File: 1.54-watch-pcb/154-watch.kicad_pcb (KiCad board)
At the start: 4 copper layers, 50 x 32.5 mm, 58 parts, among them J1 AFC24-S24FIC-00, J2 Conn_01x06_Female, J3 USB_C_Programming, J4 Jack-DC, J5 Conn_01x02_Male, Q1 Si1308, Q2 BC817, Q3 BC817, Q4 Si2301CDS, SW1 RESET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

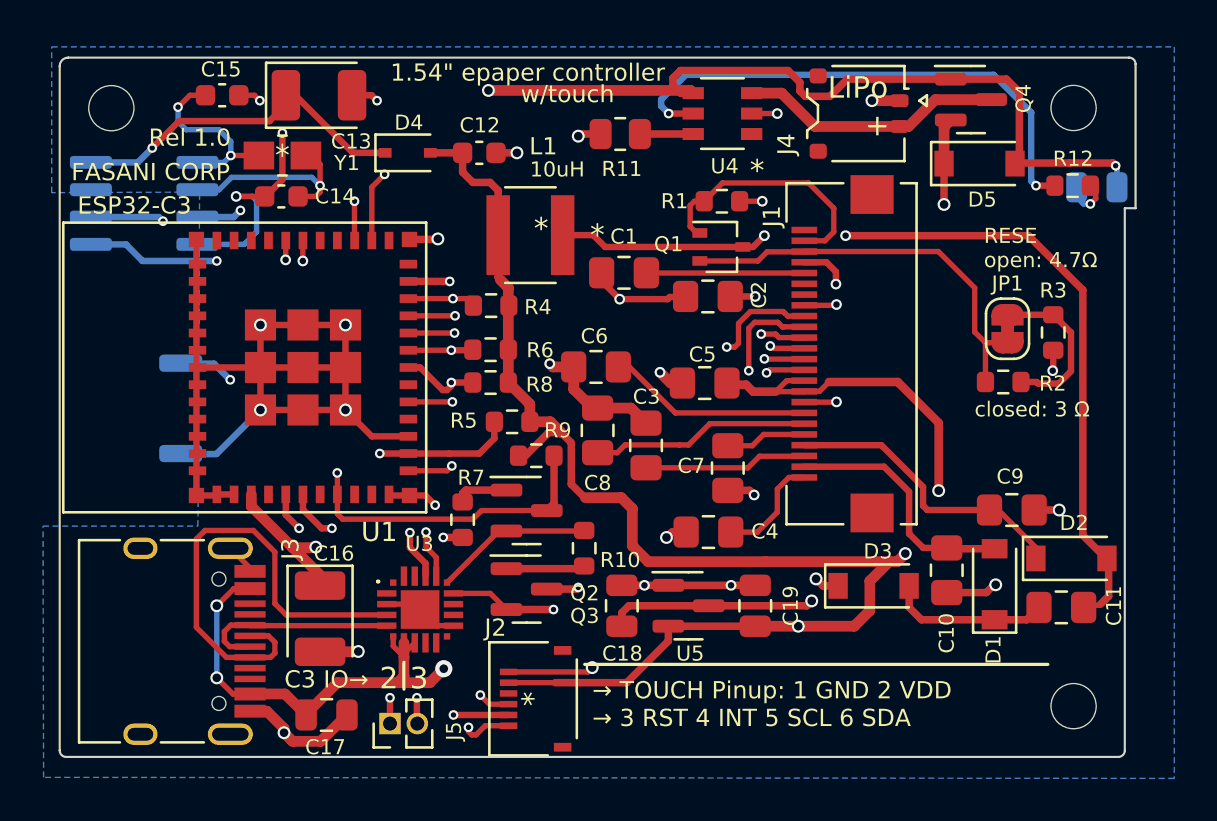
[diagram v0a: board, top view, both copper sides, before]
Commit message: RX -> TX  should be always crossed
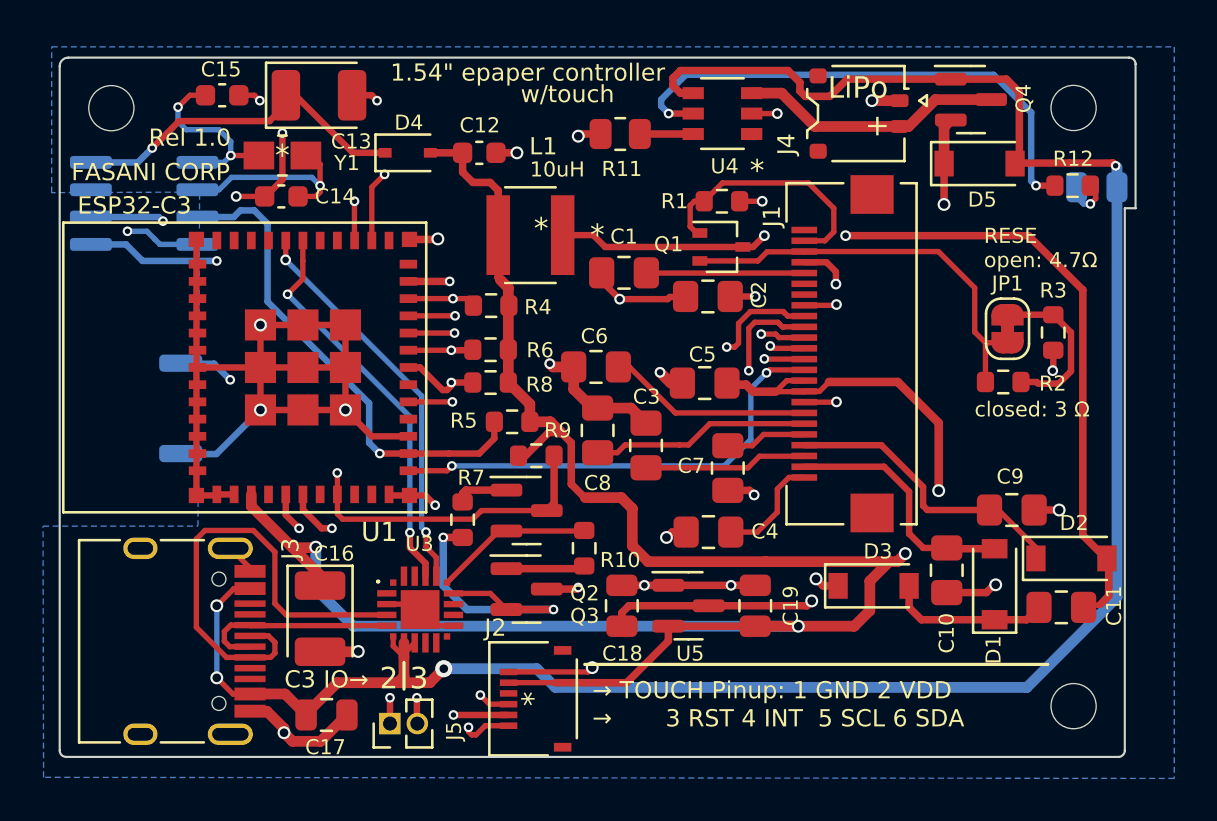
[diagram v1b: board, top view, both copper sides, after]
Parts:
- U1: value ESP32-C3-MINI -> ESP32-C3-MINI-1-N4
- U4: value SOT-23-5_TPW -> TP4057-42-SOT26-R
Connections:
- U3 pad 17: TX -> RX
- U3 pad 18: RX -> TX
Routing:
- net VBUS: track 89.8 -> 102.0 mm, vias 5 -> 4
- net GND: track 108.3 -> 106.3 mm
- net /EPD_MOSI: track 20.5 -> 21.7 mm
- net /RTC_INT: track 24.0 -> 22.9 mm, vias 2 -> 1
- net +3V3: track 111.6 -> 112.7 mm
- net /CTS: track 12.8 -> 13.7 mm
- net RX: track 19.1 -> 18.5 mm
- added copper zone on In1.Cu, net GND
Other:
- board text added: "3 RST 4 INT 5 SCL 6 SDA"
- board text added: "→ TOUCH Pinup: 1 GND 2 VDD →"
- board text removed: "→ TOUCH Pinup: 1 GND 2 VDD → 3 RST 4 INT 5 SCL 6 SDA"

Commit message: #6 update 1.54" PCB to match sample sent by GOODISPLAY
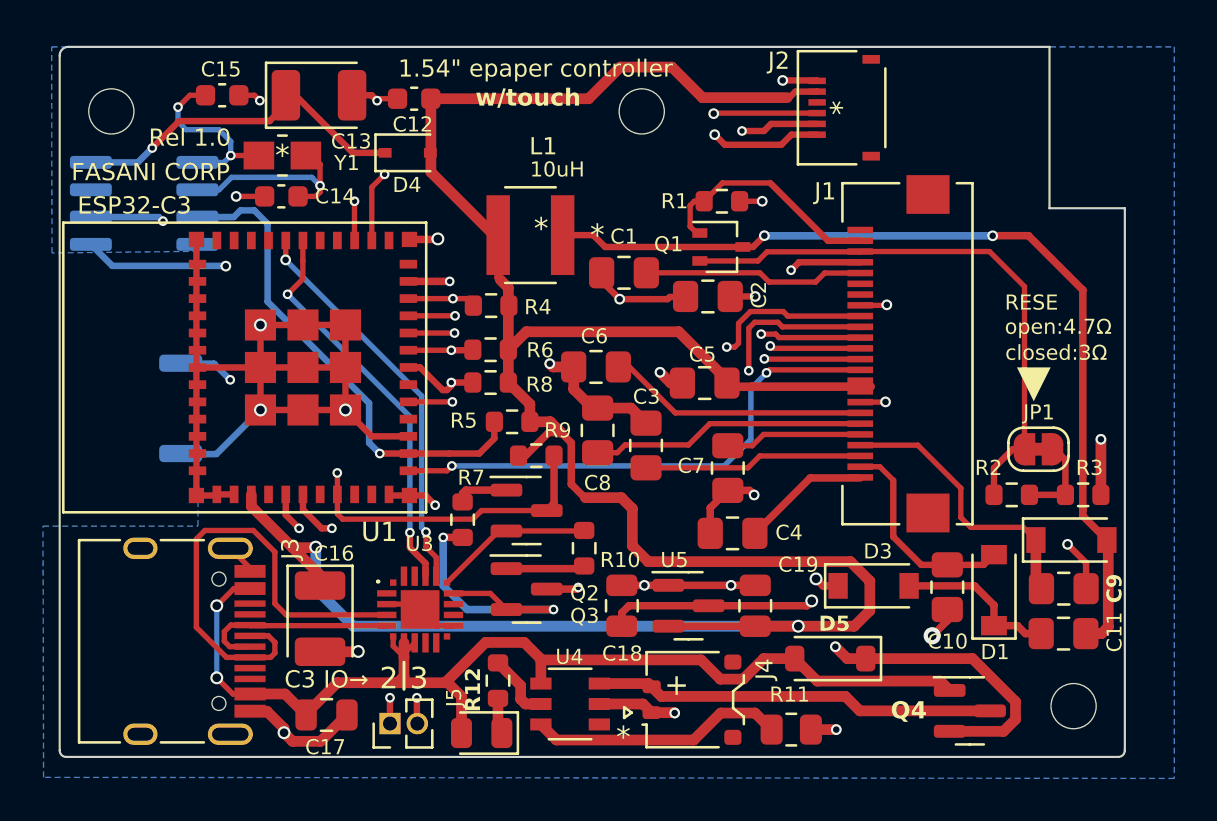
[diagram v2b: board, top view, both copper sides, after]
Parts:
- D6: moved to F.Cu
- moved D6 38.2 mm to (91.6, 61.4), turned to 180 degrees
- moved R12 35.2 mm to (92.4, 59.0), turned to -90 degrees
- moved J2 31.0 mm to (108.3, 32.3)
- moved R11 28.8 mm to (106.0, 61.2), turned to 180 degrees
- moved Q4 28.4 mm to (114.3, 60.4)
- moved U4 28.3 mm to (95.7, 60.0)
- moved J4 28.3 mm to (101.4, 59.8), turned to 90 degrees
- moved D5 24.0 mm to (107.8, 57.9), turned to 180 degrees
- moved H3 20.1 mm to (99.0, 32.5)
- moved R3 7.67 mm to (119.6, 50.3), turned to 0 degrees
- moved JP1 5.78 mm to (117.5, 48.2), turned to 0 degrees
- moved R2 5.26 mm to (116.2, 50.3)
- moved C9 4.38 mm to (118.7, 54.7)
- moved C12 3.93 mm to (88.5, 31.9), turned to 0 degrees
- moved J1 2.60 mm to (111.4, 43.8)
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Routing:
- net VBUS: track 102.0 -> 50.9 mm, vias 4 -> 2
- net Net-(U4-*STDBY): track 24.7 -> 3.15 mm, vias 2 -> 0
- net Net-(D5-K): track 37.0 -> 25.8 mm
- net Net-(U4-PROG): track 2.48 -> 11.9 mm
- net +3V3: track 112.7 -> 120.5 mm, vias 4 -> 2
- net Net-(JP1-A): track 19.3 -> 26.5 mm
- net VBAT: track 12.3 -> 18.7 mm
- net GND: track 106.3 -> 101.2 mm, vias 31 -> 26
- net Net-(JP1-B): track 7.69 -> 4.17 mm
- net Net-(C1-Pad2): track 7.35 -> 10.3 mm
- net Net-(C7-Pad2): track 3.77 -> 6.37 mm
- net Net-(C6-Pad2): track 9.53 -> 12.1 mm
- net Net-(C3-Pad2): track 7.58 -> 10.2 mm
- net /EPD_RST: track 21.2 -> 23.8 mm
- net /EPD_MOSI: track 21.7 -> 24.3 mm
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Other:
- board size 50 x 32.5 mm -> 49.5 x 33 mm
- board text added: "RESE open:4.7Ω"
- board text added: "TOUCH Pinup: 1 GND 2 VDD"
- board text added: "closed:3Ω"
- board text added: "▼"
- board text removed: "LiPo"
- board text removed: "RESE open: 4.7Ω"
- board text removed: "closed: 3 Ω"
- board text removed: "→ TOUCH Pinup: 1 GND 2 VDD →"
- board text removed: "→CHARGE RDY"

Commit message: #6 RTC errors fixed
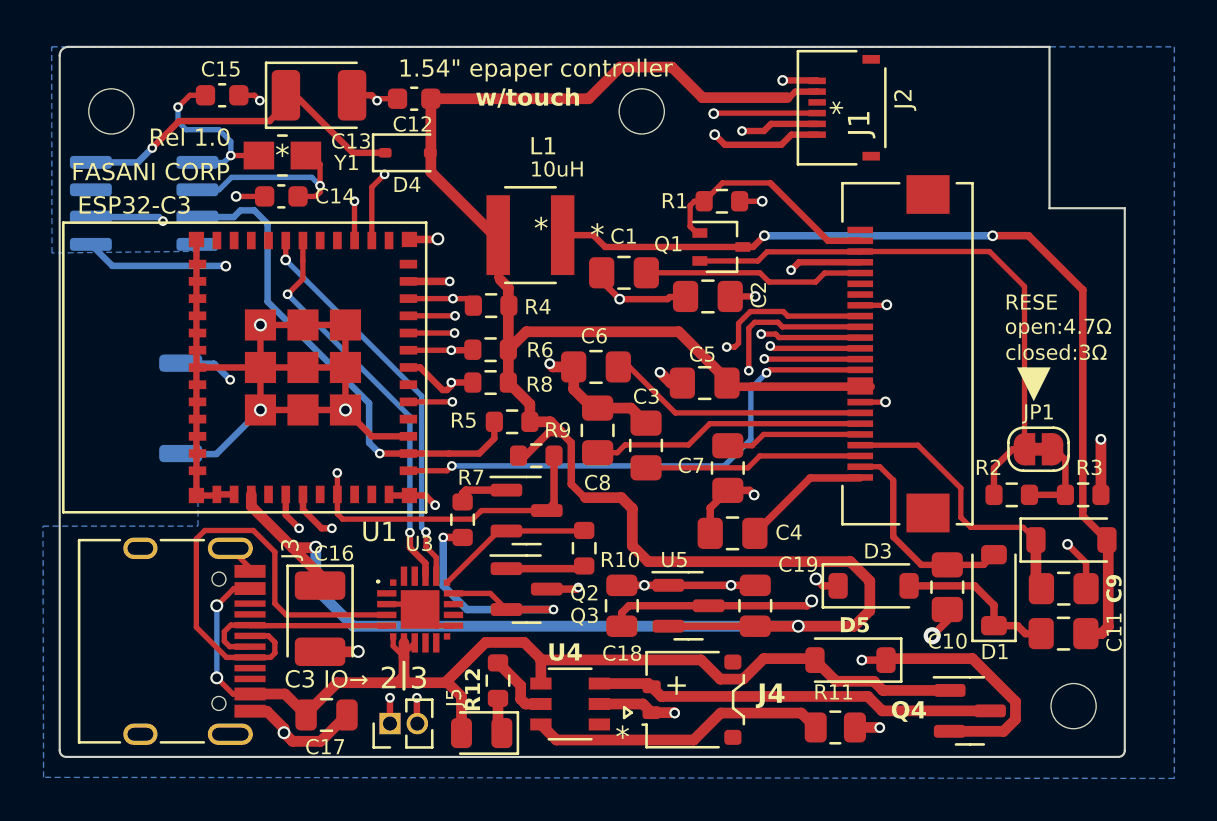
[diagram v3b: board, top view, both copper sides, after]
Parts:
- J1: value AFC24-S24FIC-00 -> CONN_AFC24-S24FIC-00_JUS
- U4: value TP4057-42-SOT26-R -> SOT-23-5_TPW
- moved R11 2.05 mm to (108.0, 61.1)
- moved D5 0.94 mm to (108.8, 58.0)
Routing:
- net Net-(U4-PROG): track 11.9 -> 13.9 mm

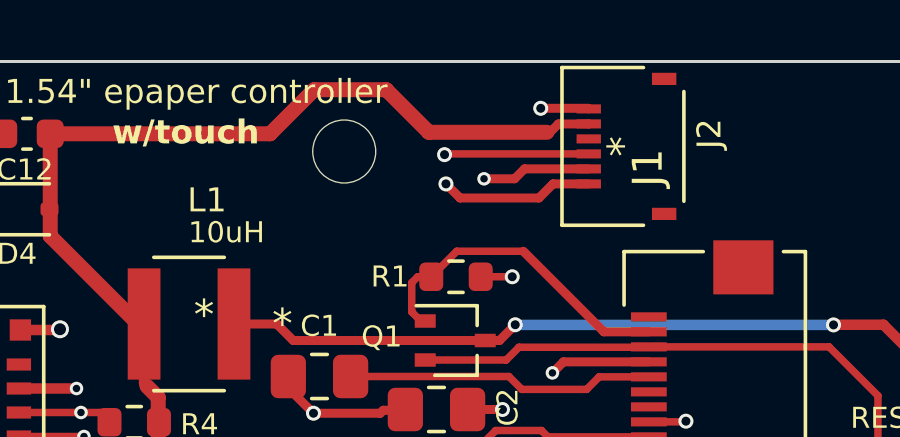
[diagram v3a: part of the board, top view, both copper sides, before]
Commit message: #6 Update touch PINUP (Was wrong)
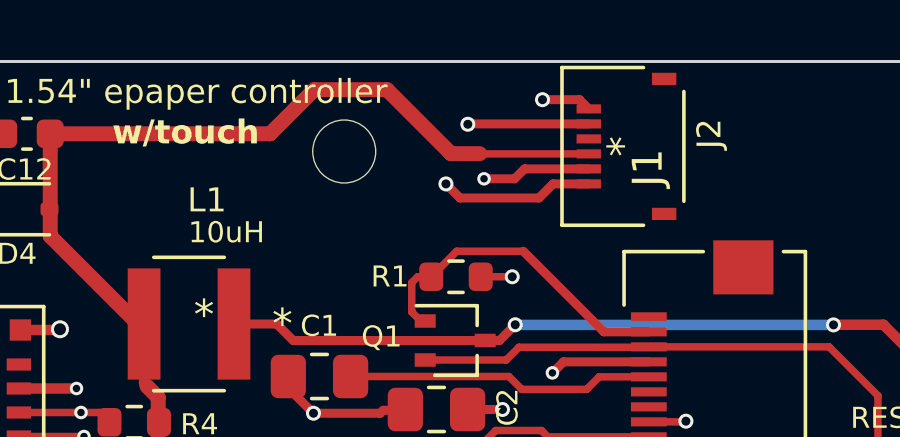
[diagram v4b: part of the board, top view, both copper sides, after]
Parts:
- J1: value CONN_AFC24-S24FIC-00_JUS -> AFC24-S24FIC-00
- U4: value SOT-23-5_TPW -> TP4057-42-SOT26-R
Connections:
- J2 pad 2: +3V3 -> /TOUCH_INT
- J2 pad 4: /TOUCH_INT -> +3V3
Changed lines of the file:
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@@
         (effects (font (size 1 1) (thickness 0.15)))
     )
-    (fp_text value "CONN_AFC24-S24FIC-00_JUS" (at 0.49 4 90) (layer "F.SilkS") hide
+    (fp_text value "AFC24-S24FIC-00" (at 0.49 4 90) (layer "F.SilkS") hide
         (effects (font (size 1 1) (thickness 0.15)))
     )
@@
       (net 2 "GND") (pinfunction "Pin_1") (pintype "passive"))
     (pad "2" smd rect (at 0.750001 -1.139 90) (size 0.3048 0.8128) (layers "F.Cu" "F.Paste" "F.Mask")
-      (net 4 "+3V3") (pinfunction "Pin_2") (pintype "passive"))
+      (net 36 "/TOUCH_INT") (pinfunction "Pin_2") (pintype "passive"))
     (pad "3" smd rect (at 0.249999 -1.139 90) (size 0.3048 0.8128) (layers "F.Cu" "F.Paste" "F.Mask")
       (net 31 "unconnected-(J2-Pin_3-Pad3)") (pinfunction "Pin_3") (pintype "passive+no_connect"))
     (pad "4" smd rect (at -0.25 -1.139 90) (size 0.3048 0.8128) (layers "F.Cu" "F.Paste" "F.Mask")
-      (net 36 "/TOUCH_INT") (pinfunction "Pin_4") (pintype "passive"))
+      (net 4 "+3V3") (pinfunction "Pin_4") (pintype "passive"))
     (pad "5" smd rect (at -0.750001 -1.139 90) (size 0.3048 0.8128) (layers "F.Cu" "F.Paste" "F.Mask")
       (net 34 "/I2C_SCL") (pinfunction "Pin_5") (pintype "passive"))
@@
         (effects (font (size 0.8 0.8) (thickness 0.14) bold))
     )
-    (fp_text value "SOT-23-5_TPW" (at 0.09 6.52 180) (layer "F.SilkS") hide
+    (fp_text value "TP4057-42-SOT26-R" (at 0.09 6.52 180) (layer "F.SilkS") hide
         (effects (font (size 1 1) (thickness 0.15)))
     )
@@
   (segment (start 80.845 53.875) (end 80.845 53.72) (width 0.25) (layer "F.Cu") (net 2))
   (segment (start 86.5 31.75) (end 86.75 32) (width 0.3) (layer "F.Cu") (net 2))
-  (segment (start 107.181 31.06) (end 105.6 31.06) (width 0.3) (layer "F.Cu") (net 2))
   (segment (start 89.55 38.45) (end 89.575 38.425) (width 0.35) (layer "F.Cu") (net 2))
   (segment (start 104.0625 50.1125) (end 104.275 50.325) (width 0.35) (layer "F.Cu") (net 2))
@@
   (segment (start 98.025 41.225) (end 100.25 41.225) (width 0.3) (layer "F.Cu") (net 2))
   (segment (start 113.25 56.17) (end 112.55 56.87) (width 0.35) (layer "F.Cu") (net 2))
-  (segment (start 107.201 31.08) (end 107.181 31.06) (width 0.3) (layer "F.Cu") (net 2))
   (segment (start 103.2 54.525) (end 104.325 54.525) (width 0.35) (layer "F.Cu") (net 2))
+  (segment (start 106.8935 30.7725) (end 105.658781 30.7725) (width 0.3) (layer "F.Cu") (net 2))
   (segment (start 98.55 46.2875) (end 99.25 46.9875) (width 0.5) (layer "F.Cu") (net 2))
   (segment (start 120.39 50.32) (end 120.39 47.74) (width 0.5) (layer "F.Cu") (net 2))
@@
   (segment (start 110.367999 46.012001) (end 110.38 46) (width 0.25) (layer "F.Cu") (net 2))
   (segment (start 103.6 36.675) (end 104.65 36.675) (width 0.25) (layer "F.Cu") (net 2))
+  (segment (start 107.201 31.08) (end 106.8935 30.7725) (width 0.3) (layer "F.Cu") (net 2))
   (segment (start 100.9375 45.125) (end 100.4 45.125) (width 0.5) (layer "F.Cu") (net 2))
   (segment (start 85.2801 46.375) (end 81.3301 46.375) (width 0.3) (layer "F.Cu") (net 2))
@@
   (via (at 94.775 44.225) (size 0.5) (drill 0.3) (layers "F.Cu" "B.Cu") (net 2))
   (via (at 99.175 54.525) (size 0.5) (drill 0.3) (layers "F.Cu" "B.Cu") (net 2))
-  (via (at 105.6 31.06) (size 0.5) (drill 0.3) (layers "F.Cu" "B.Cu") (net 2))
+  (via (at 105.658781 30.7725) (size 0.5) (drill 0.3) (layers "F.Cu" "B.Cu") (net 2))
   (via (at 81.3301 42.425) (size 0.6) (drill 0.4) (layers "F.Cu" "B.Cu") (net 2))
   (via (at 89.45 50.8) (size 0.45) (drill 0.25) (layers "F.Cu" "B.Cu") (net 2))
@@
   (segment (start 79.3 55.475) (end 79.3 58.825) (width 0.25) (layer "B.Cu") (net 3))
   (segment (start 98.6125 50.9625) (end 98.6125 52.6875) (width 0.5) (layer "F.Cu") (net 4))
-  (segment (start 101.87 31.86) (end 105.81 31.86) (width 0.5) (layer "F.Cu") (net 4))
   (segment (start 96.425 50.45) (end 98.1 50.45) (width 0.5) (layer "F.Cu") (net 4))
   (segment (start 104.186137 45.296137) (end 103.183637 45.296137) (width 0.4) (layer "F.Cu") (net 4))
@@
   (segment (start 95.775 49.825) (end 96.4 50.45) (width 0.35) (layer "F.Cu") (net 4))
   (segment (start 96.4 50.45) (end 96.425 50.45) (width 0.35) (layer "F.Cu") (net 4))
-  (segment (start 89.25 31.91) (end 96.58 31.91) (width 0.5) (layer "F.Cu") (net 4))
   (segment (start 103.0125 45.125) (end 103.0125 44.9825) (width 0.5) (layer "F.Cu") (net 4))
   (segment (start 108.75 53.425) (end 109.65 54.325) (width 0.5) (layer "F.Cu") (net 4))
   (segment (start 103.0125 44.9825) (end 100.77 42.74) (width 0.5) (layer "F.Cu") (net 4))
   (segment (start 93.325 48.5) (end 93.65 48.5) (width 0.35) (layer "F.Cu") (net 4))
+  (segment (start 102.61 32.572) (end 103.57 32.572) (width 0.5) (layer "F.Cu") (net 4))
+  (segment (start 103.578 32.58) (end 103.57 32.572) (width 0.25) (layer "F.Cu") (net 4))
   (segment (start 93.85 46.1) (end 93.85 46.925) (width 0.5) (layer "F.Cu") (net 4))
   (segment (start 109.65 55.7) (end 108.925 56.425) (width 0.5) (layer "F.Cu") (net 4))
+  (segment (start 107.201 32.58) (end 103.578 32.58) (width 0.25) (layer "F.Cu") (net 4))
   (segment (start 80.9051 50.8551) (end 82.825 52.775) (width 0.5) (layer "F.Cu") (net 4))
   (segment (start 104.192274 45.29) (end 109.69 45.29) (width 0.4) (layer "F.Cu") (net 4))
   (segment (start 92.3778 40.2278) (end 92.475 40.325) (width 0.35) (layer "F.Cu") (net 4))
+  (segment (start 89.25 31.91) (end 96.58 31.91) (width 0.5) (layer "F.Cu") (net 4))
   (segment (start 84.1 54.05) (end 84.1 54.5375) (width 0.5) (layer "F.Cu") (net 4))
   (segment (start 92.3778 38.25) (end 92.3778 40.2278) (width 0.35) (layer "F.Cu") (net 4))
+  (segment (start 98.05 30.44) (end 100.478 30.44) (width 0.5) (layer "F.Cu") (net 4))
+  (segment (start 100.478 30.44) (end 102.61 32.572) (width 0.5) (layer "F.Cu") (net 4))
   (segment (start 108.925 56.425) (end 106.325 56.425) (width 0.5) (layer "F.Cu") (net 4))
-  (segment (start 106.187399 31.582601) (end 105.86 31.91) (width 0.3) (layer "F.Cu") (net 4))
   (segment (start 106.325 56.425) (end 104.325 56.425) (width 0.5) (layer "F.Cu") (net 4))
   (segment (start 95.3 47.425) (end 95.775 47.9) (width 0.35) (layer "F.Cu") (net 4))
@@
   (segment (start 93.65 48.5) (end 94.725 47.425) (width 0.35) (layer "F.Cu") (net 4))
   (segment (start 92.85 45.1) (end 93.85 46.1) (width 0.5) (layer "F.Cu") (net 4))
-  (segment (start 100.45 30.44) (end 101.87 31.86) (width 0.5) (layer "F.Cu") (net 4))
-  (segment (start 98.05 30.44) (end 100.45 30.44) (width 0.5) (layer "F.Cu") (net 4))
-  (segment (start 96.58 31.91) (end 98.05 30.44) (width 0.5) (layer "F.Cu") (net 4))
   (segment (start 82.825 52.775) (end 84.1 54.05) (width 0.5) (layer "F.Cu") (net 4))
   (segment (start 83.875 52.775) (end 83.9 52.75) (width 0.5) (layer "F.Cu") (net 4))
   (segment (start 98.1 50.45) (end 98.6125 50.9625) (width 0.5) (layer "F.Cu") (net 4))
   (segment (start 92.85 45.1) (end 92.85 40.7) (width 0.5) (layer "F.Cu") (net 4))
-  (segment (start 107.198398 31.582601) (end 106.187399 31.582601) (width 0.3) (layer "F.Cu") (net 4))
+  (segment (start 96.58 31.91) (end 98.05 30.44) (width 0.5) (layer "F.Cu") (net 4))
   (segment (start 98.6125 52.6875) (end 99.35 53.425) (width 0.5) (layer "F.Cu") (net 4))
   (segment (start 93.85 46.925) (end 94.8 46.925) (width 0.5) (layer "F.Cu") (net 4))
   (segment (start 109.65 54.325) (end 109.65 55.7) (width 0.5) (layer "F.Cu") (net 4))
   (segment (start 93.685 42.74) (end 92.85 43.575) (width 0.5) (layer "F.Cu") (net 4))
-  (segment (start 107.201 31.579999) (end 107.198398 31.582601) (width 0.3) (layer "F.Cu") (net 4))
   (segment (start 99.35 53.425) (end 108.75 53.425) (width 0.5) (layer "F.Cu") (net 4))
   (via (at 83.9 52.75) (size 0.6) (drill 0.4) (layers "F.Cu" "B.Cu") (net 4))
@@
   (segment (start 76.61 37.41) (end 76.8 37.6) (width 0.3) (layer "B.Cu") (net 34))
   (segment (start 90.900001 41.200001) (end 91.225 41.525) (width 0.25) (layer "F.Cu") (net 36))
-  (segment (start 102.418063 32.58) (end 102.393563 32.6045) (width 0.25) (layer "F.Cu") (net 36))
-  (segment (start 107.201 32.58) (end 102.418063 32.58) (width 0.25) (layer "F.Cu") (net 36))
+  (segment (start 107.201 31.579999) (end 103.182001 31.579999) (width 0.3) (layer "F.Cu") (net 36))
   (segment (start 88.2051 41.200001) (end 90.274999 41.200001) (width 0.25) (layer "F.Cu") (net 36))
   (segment (start 90.274999 41.200001) (end 90.900001 41.200001) (width 0.25) (layer "F.Cu") (net 36))
+  (segment (start 103.182001 31.579999) (end 103.17 31.592) (width 0.3) (layer "F.Cu") (net 36))
+  (via (at 103.17 31.592) (size 0.5) (drill 0.3) (layers "F.Cu" "B.Cu") (net 36))
   (via (at 90.274999 41.200001) (size 0.45) (drill 0.25) (layers "F.Cu" "B.Cu") (net 36))
-  (via (at 102.393563 32.6045) (size 0.5) (drill 0.3) (layers "F.Cu" "B.Cu") (net 36))
-  (segment (start 102.1655 32.6045) (end 93.569999 41.200001) (width 0.25) (layer "In2.Cu") (net 36))
-  (segment (start 102.376787 32.587724) (end 102.393563 32.6045) (width 0.25) (layer "In2.Cu") (net 36))
+  (segment (start 103.17 31.592) (end 93.569999 41.192001) (width 0.3) (layer "In2.Cu") (net 36))
+  (segment (start 93.569999 41.192001) (end 93.569999 41.200001) (width 0.3) (layer "In2.Cu") (net 36))
   (segment (start 93.569999 41.200001) (end 90.274999 41.200001) (width 0.25) (layer "In2.Cu") (net 36))
-  (segment (start 102.393563 32.6045) (end 102.1655 32.6045) (width 0.25) (layer "In2.Cu") (net 36))
   (segment (start 78.75 51.975) (end 81 51.975) (width 0.25) (layer "F.Cu") (net 37))
   (segment (start 80.845 56.875) (end 81.7 56.875) (width 0.25) (layer "F.Cu") (net 37))
